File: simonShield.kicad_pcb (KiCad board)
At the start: 2 copper layers, 83 x 64 mm, 44 parts, among them P1 PWR_JUMPER, Q1 BC547, Q2 BC547, Q3 BC547, Q4 BC547, Q5 BC547, SW1 SW_PUSH, SW2 SW_PUSH, SW3 SW_PUSH, SW4 SW_PUSH, SW5 SW_PUSH, SW6 SW_PUSH, SW7 SW_PUSH, SW8 SW_PUSH, U1 BUZZER

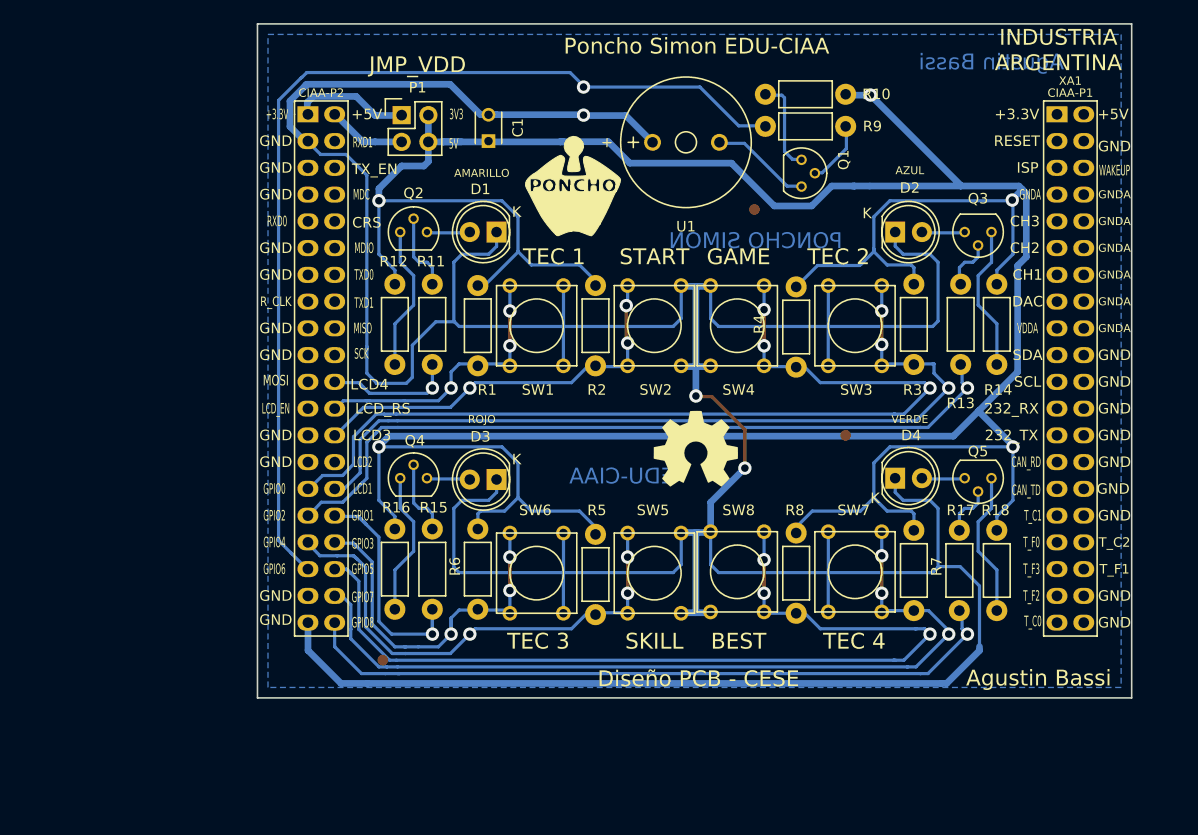
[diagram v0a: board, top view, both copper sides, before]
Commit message: Version 1 practicamente terminada de poncho Simon con EDU CIAA.
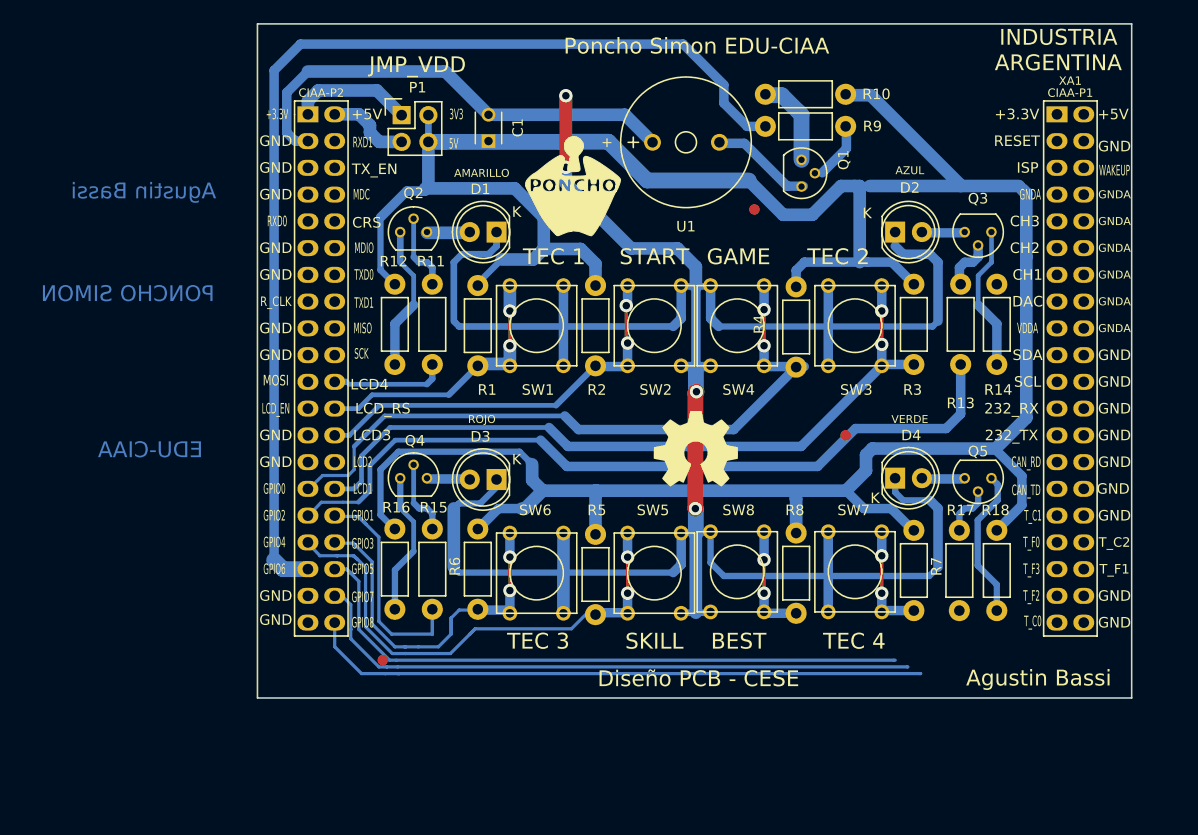
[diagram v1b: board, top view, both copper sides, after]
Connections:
- F1 pad 1: (no net) -> Net-(F1-Pad1)
- F2 pad 1: (no net) -> Net-(F2-Pad1)
- F3 pad 1: (no net) -> Net-(F3-Pad1)
- XA1 pad 1: (no net) -> Net-(XA1-Pad1)
- XA1 pad 10: (no net) -> Net-(XA1-Pad10)
- XA1 pad 11: (no net) -> Net-(XA1-Pad11)
- XA1 pad 12: (no net) -> Net-(XA1-Pad12)
- XA1 pad 13: (no net) -> Net-(XA1-Pad13)
- XA1 pad 14: (no net) -> Net-(XA1-Pad14)
- XA1 pad 15: (no net) -> Net-(XA1-Pad15)
- XA1 pad 16: (no net) -> Net-(XA1-Pad16)
- XA1 pad 17: (no net) -> Net-(XA1-Pad17)
- XA1 pad 18: (no net) -> Net-(XA1-Pad18)
- XA1 pad 19: (no net) -> Net-(XA1-Pad19)
- XA1 pad 2: (no net) -> Net-(XA1-Pad2)
- XA1 pad 20: (no net) -> Net-(XA1-Pad20)
- XA1 pad 21: (no net) -> Net-(XA1-Pad21)
- XA1 pad 22: (no net) -> Net-(XA1-Pad22)
- XA1 pad 23: (no net) -> Net-(XA1-Pad23)
- XA1 pad 24: (no net) -> Net-(XA1-Pad24)
- XA1 pad 25: (no net) -> Net-(XA1-Pad25)
- XA1 pad 26: (no net) -> Net-(XA1-Pad26)
- XA1 pad 27: (no net) -> Net-(XA1-Pad27)
- XA1 pad 28: (no net) -> Net-(XA1-Pad28)
- XA1 pad 29: (no net) -> Net-(XA1-Pad29)
- XA1 pad 3: (no net) -> Net-(XA1-Pad3)
- XA1 pad 30: (no net) -> Net-(XA1-Pad30)
- XA1 pad 31: (no net) -> Net-(XA1-Pad31)
- XA1 pad 32: (no net) -> Net-(XA1-Pad32)
- XA1 pad 33: (no net) -> Net-(XA1-Pad33)
- XA1 pad 34: (no net) -> Net-(XA1-Pad34)
- XA1 pad 35: (no net) -> Net-(XA1-Pad35)
- XA1 pad 36: (no net) -> Net-(XA1-Pad36)
- XA1 pad 37: (no net) -> Net-(XA1-Pad37)
- XA1 pad 38: (no net) -> Net-(XA1-Pad38)
- XA1 pad 39: (no net) -> Net-(XA1-Pad39)
- XA1 pad 4: (no net) -> Net-(XA1-Pad4)
- XA1 pad 40: (no net) -> Net-(XA1-Pad40)
- XA1 pad 44: (no net) -> Net-(XA1-Pad44)
- XA1 pad 45: (no net) -> Net-(XA1-Pad45)
- XA1 pad 46: (no net) -> Net-(XA1-Pad46)
- XA1 pad 47: (no net) -> Net-(XA1-Pad47)
- XA1 pad 48: (no net) -> Net-(XA1-Pad48)
- XA1 pad 49: (no net) -> Net-(XA1-Pad49)
- XA1 pad 5: (no net) -> Net-(XA1-Pad5)
- XA1 pad 50: (no net) -> Net-(XA1-Pad50)
- XA1 pad 51: (no net) -> Net-(XA1-Pad51)
- XA1 pad 52: (no net) -> Net-(XA1-Pad52)
- XA1 pad 53: (no net) -> Net-(XA1-Pad53)
- XA1 pad 54: (no net) -> Net-(XA1-Pad54)
- XA1 pad 55: (no net) -> Net-(XA1-Pad55)
- XA1 pad 56: (no net) -> Net-(XA1-Pad56)
- XA1 pad 57: (no net) -> Net-(XA1-Pad57)
- XA1 pad 58: (no net) -> Net-(XA1-Pad58)
- XA1 pad 59: (no net) -> Net-(XA1-Pad59)
- XA1 pad 6: (no net) -> Net-(XA1-Pad6)
- XA1 pad 60: (no net) -> Net-(XA1-Pad60)
- XA1 pad 61: (no net) -> Net-(XA1-Pad61)
- XA1 pad 63: (no net) -> Net-(XA1-Pad63)
- XA1 pad 65: (no net) -> Net-(XA1-Pad65)
- XA1 pad 67: (no net) -> Net-(XA1-Pad67)
- XA1 pad 68: (no net) -> Net-(XA1-Pad68)
- XA1 pad 7: (no net) -> Net-(XA1-Pad7)
- XA1 pad 8: (no net) -> Net-(XA1-Pad8)
- XA1 pad 9: (no net) -> Net-(XA1-Pad9)
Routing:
- net GND: track 385.3 -> 292.9 mm, vias 3 -> 4
- net VCC: track 339.8 -> 280.5 mm, vias 5 -> 0
- net /buttons/BTN_CFG_2: track 88.9 -> 64.9 mm, vias 3 -> 2
- net /buttons/BTN_CFG_4: track 88.8 -> 70.8 mm, vias 3 -> 2
- net /buttons/BTN_LED_4: track 78.7 -> 69.1 mm, vias 3 -> 2
- net /buttons/BTN_LED_2: track 80.2 -> 70.8 mm, vias 3 -> 2
- net /ciaaConector/LED_4: track 68.6 -> 59.3 mm, vias 1 -> 0
- net /ciaaConector/PWM: track 96.1 -> 102.0 mm, vias 1 -> 0
- net /ciaaConector/LED_1: track 13.2 -> 10.9 mm, vias 1 -> 0
- net /ciaaConector/LED_2: track 72.7 -> 74.5 mm, vias 1 -> 0
- net /buttons/BTN_LED_1: track 27.1 -> 26.0 mm, vias 3 -> 2
- net Net-(Q5-Pad1): track 13.7 -> 14.4 mm
- net Net-(Q1-Pad1): track 9.06 -> 8.43 mm
- net /buttons/BTN_CFG_1: track 38.6 -> 38.3 mm, vias 3 -> 2
- net /ciaaConector/LED_3: vias 1 -> 0
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- removed copper zone on B.Cu, net GND
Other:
- net class Default: clearance 0.3048 -> 0.3; trace_width 0.3048 -> 0.3
- rule trace_clearance: 0.3048 -> 0.3
- rule trace_min: 0.3048 -> 0.3

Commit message: Version luego de cambiar los pines y agregar dos resistencias de puentes.@
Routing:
- net /ciaaConector/PWM: track 102.0 -> 66.9 mm
- net /ciaaConector/LED_4: track 59.3 -> 81.8 mm
- net /buttons/BTN_CFG_4: track 70.8 -> 57.9 mm
- net /buttons/BTN_LED_4: track 69.1 -> 81.3 mm
- net /ciaaConector/LED_2: track 74.5 -> 64.2 mm
- net /ciaaConector/LED_3: track 24.2 -> 14.5 mm
- net /buttons/BTN_CFG_2: track 64.9 -> 56.2 mm
- net /buttons/BTN_LED_3: track 48.7 -> 40.4 mm
- net /buttons/BTN_CFG_3: track 36.4 -> 28.9 mm
- net /buttons/BTN_LED_2: track 70.8 -> 64.5 mm
- net /buttons/BTN_CFG_1: track 38.3 -> 35.4 mm
- net /ciaaConector/LED_1: track 10.9 -> 12.5 mm

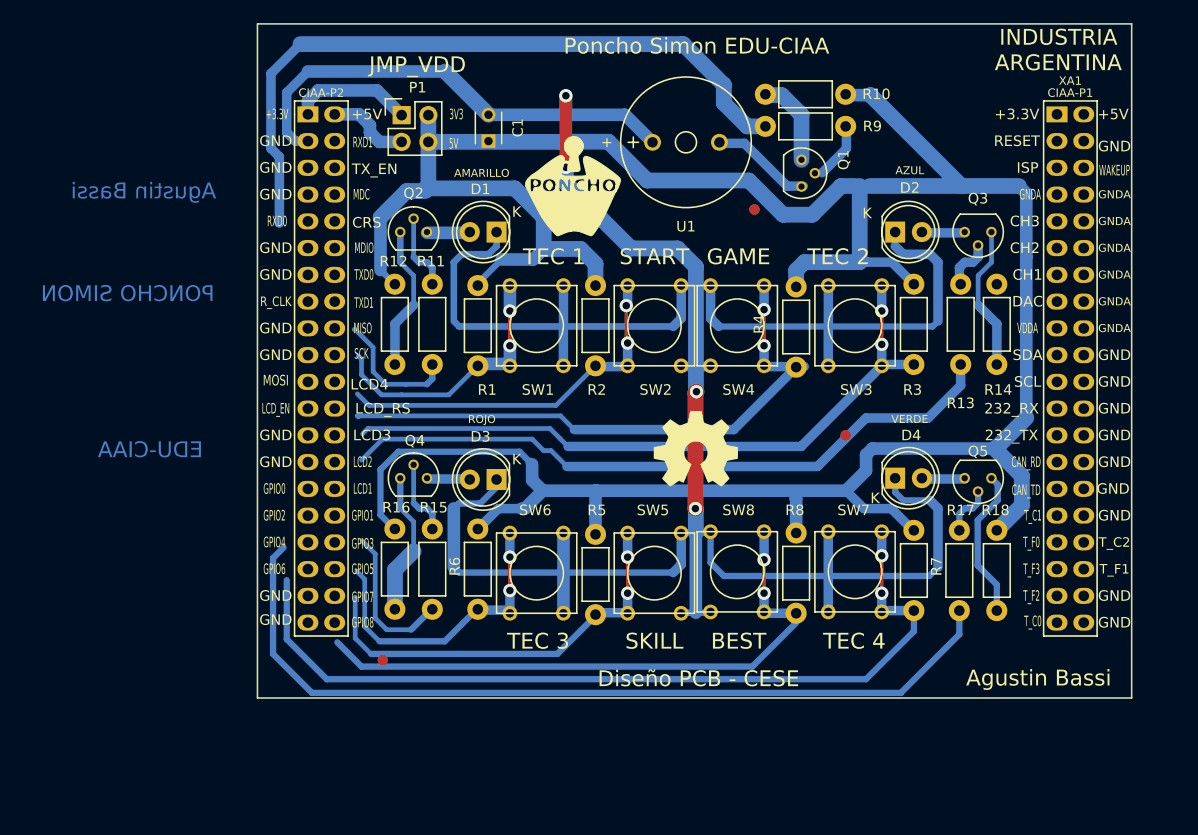
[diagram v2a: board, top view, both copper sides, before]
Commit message: Version totalmente ruteada. Previo a hacer puentes con resistencia y a serigrafia.
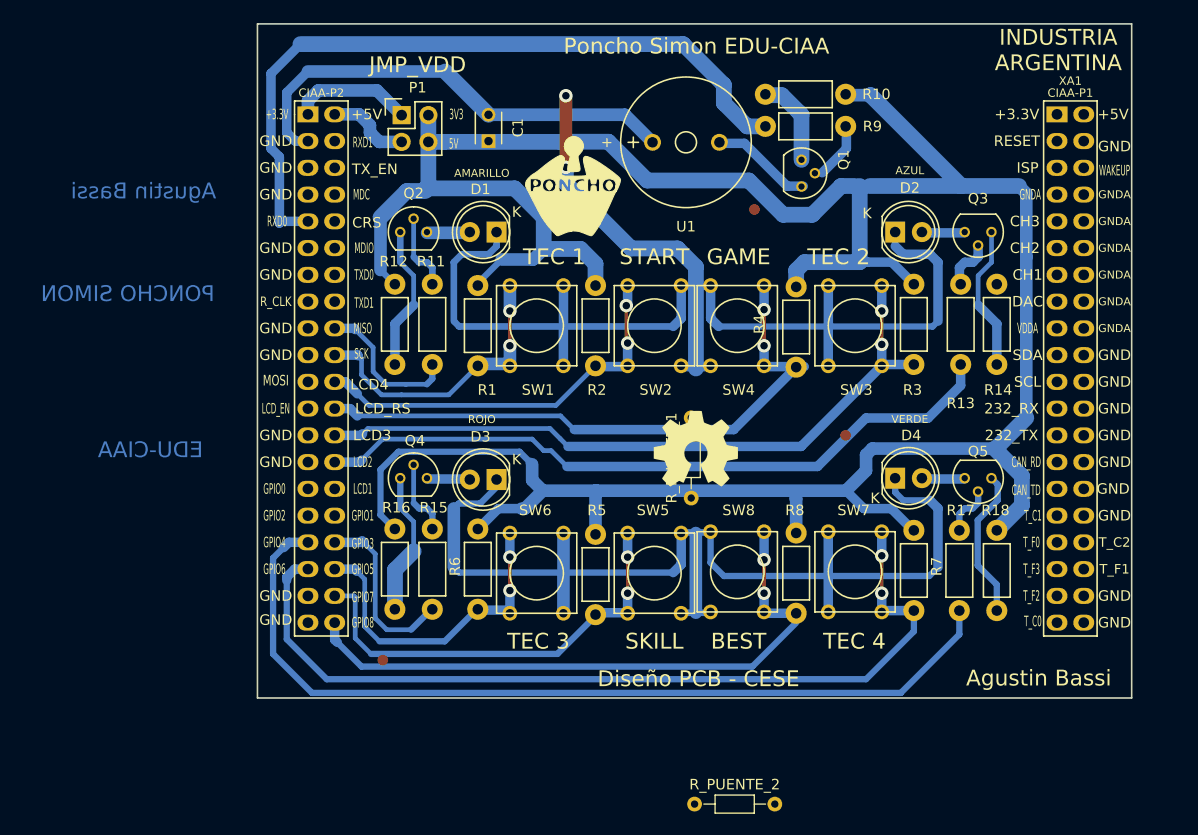
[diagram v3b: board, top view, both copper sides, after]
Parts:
- added R_PUENTE_1: R, Resistors_THT:R_Axial_DIN0204_L3.6mm_D1.6mm_P7.62mm_Horizontal, F.Cu at (154.5, 97.9)
- added R_PUENTE_2: R, Resistors_THT:R_Axial_DIN0204_L3.6mm_D1.6mm_P7.62mm_Horizontal, F.Cu at (154.8, 127.0)
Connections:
- XA1 pad 49: Net-(XA1-Pad49) -> /ciaaConector/PWM
- XA1 pad 58: Net-(XA1-Pad58) -> /ciaaConector/LED_1
- XA1 pad 60: Net-(XA1-Pad60) -> /buttons/BTN_LED_1
- XA1 pad 62: /ciaaConector/LED_1 -> /buttons/BTN_CFG_1
- XA1 pad 64: /buttons/BTN_LED_1 -> /buttons/BTN_CFG_2
- XA1 pad 66: /buttons/BTN_CFG_1 -> /buttons/BTN_LED_2
- XA1 pad 68: Net-(XA1-Pad68) -> /ciaaConector/LED_2
- XA1 pad 69: /buttons/BTN_CFG_2 -> Net-(XA1-Pad69)
- XA1 pad 70: /buttons/BTN_LED_2 -> Net-(XA1-Pad70)
- XA1 pad 71: /ciaaConector/LED_2 -> Net-(XA1-Pad71)
- XA1 pad 72: /ciaaConector/LED_3 -> Net-(XA1-Pad72)
- XA1 pad 73: /buttons/BTN_LED_3 -> /ciaaConector/LED_4
- XA1 pad 74: /buttons/BTN_CFG_3 -> /ciaaConector/LED_3
- XA1 pad 75: /ciaaConector/PWM -> /buttons/BTN_LED_4
- XA1 pad 76: /buttons/BTN_CFG_4 -> /buttons/BTN_CFG_3
- XA1 pad 78: /buttons/BTN_LED_4 -> /buttons/BTN_LED_3
- XA1 pad 80: /ciaaConector/LED_4 -> /buttons/BTN_CFG_4
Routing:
- net GND: track 292.9 -> 277.2 mm, vias 4 -> 2
- net /ciaaConector/LED_3: track 14.5 -> 17.5 mm
- net /ciaaConector/PWM: track 66.9 -> 69.8 mm
- net /buttons/BTN_LED_2: track 64.5 -> 67.2 mm
- net /ciaaConector/LED_2: track 64.2 -> 66.9 mm
- net /buttons/BTN_LED_4: track 81.3 -> 83.9 mm
- net /buttons/BTN_CFG_1: track 35.4 -> 38.0 mm
- net /ciaaConector/LED_4: track 81.8 -> 84.3 mm
- net /buttons/BTN_CFG_2: track 56.2 -> 58.7 mm
- net /buttons/BTN_LED_1: track 25.7 -> 27.9 mm
- net /buttons/BTN_CFG_3: track 28.9 -> 31.1 mm
- net /ciaaConector/LED_1: track 12.5 -> 14.5 mm
- net /buttons/BTN_LED_3: track 40.4 -> 42.4 mm
- net /buttons/BTN_CFG_4: track 57.9 -> 59.8 mm

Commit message: Commit de acomodo de directorio. Previo a generar los gerbers de fabricacion final.
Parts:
- removed R_PUENTE_1, R_PUENTE_2: R, Resistors_THT:R_Axial_DIN0204_L3.6mm_D1.6mm_P7.62mm_Horizontal
- added R 0 Ohm: R, Resistors_THT:R_Axial_DIN0207_L6.3mm_D2.5mm_P10.16mm_Horizontal, F.Cu at (145.4, 68.8)
- added R 0 Ohm: R, Resistors_THT:R_Axial_DIN0207_L6.3mm_D2.5mm_P10.16mm_Horizontal, F.Cu at (155.0, 99.0)
- D1, D2, D3, D4: footprint footprints:LED-5MM -> simonShield:LED-5MM
- F1, F2, F3: footprint footprints:Fiducial_1mm -> simonShield:Fiducial_1mm
- P1: footprint footprints:Pin_Header_Straight_2x02 -> simonShield:Pin_Header_Straight_2x02
- Q1, Q2, Q3, Q4, Q5: footprint footprints:TO-92_Molded_Narrow -> simonShield:TO-92_Molded_Narrow
- R1, R10, R11, R12, R13, R14, R15, R16, R17, R18, R2, R3, R5, R6, R7, R8, R9: footprint footprints:Resistor_Horizontal_RM7mm -> simonShield:Resistor_Horizontal_RM7mm
- SW1, SW2, SW3, SW4, SW5, SW6, SW7, SW8: footprint footprints:SW_PUSH_SMALL -> simonShield:SW_PUSH_SMALL
- U1: footprint footprints:MagneticBuzzer_ProSignal_ABT-410-RC -> simonShield:MagneticBuzzer_ProSignal_ABT-410-RC
- moved G*** 34.8 mm to (177.0, 60.0)
- moved G101 7.44 mm to (147.5, 93.0)
- moved F3 1.94 mm to (167.2, 92.2)
- moved F1 1.03 mm to (125.2, 112.2)
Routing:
- net GND: track 277.2 -> 268.0 mm, vias 2 -> 0
- net VCC: track 280.5 -> 282.4 mm
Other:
- board size 83 x 64 mm -> 83.2 x 65.2 mm
- board text added: "Autor Agustin Bassi"
- board text added: "Autor: Juan Agustin Bassi git@gitlab.com:abassi/ponchoSimon.git"
- board text added: "EDU-CIAA NXP"
- board text added: "PONCHO JUEGO SIMON"
- board text added: "Poncho juego Simon EDU-CIAA NXP"
- board text removed: "Agustin Bassi"
- board text removed: "Diseño PCB - CESE"
- board text removed: "EDU-CIAA"
- board text removed: "PONCHO SIMON"
- board text removed: "Poncho Simon EDU-CIAA"
